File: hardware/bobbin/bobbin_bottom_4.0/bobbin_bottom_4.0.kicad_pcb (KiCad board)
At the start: 2 copper layers, 90.5 x 8.5 mm, 2 parts

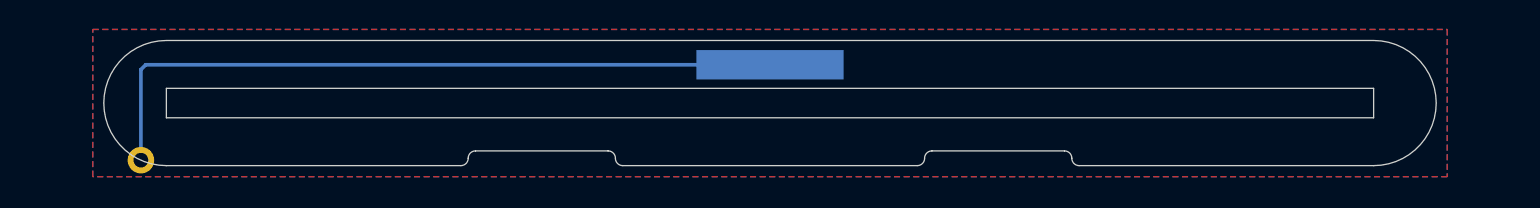
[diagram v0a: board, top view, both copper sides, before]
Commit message: Preamp, Tone Block, Passive, and Bobbin Panel updates
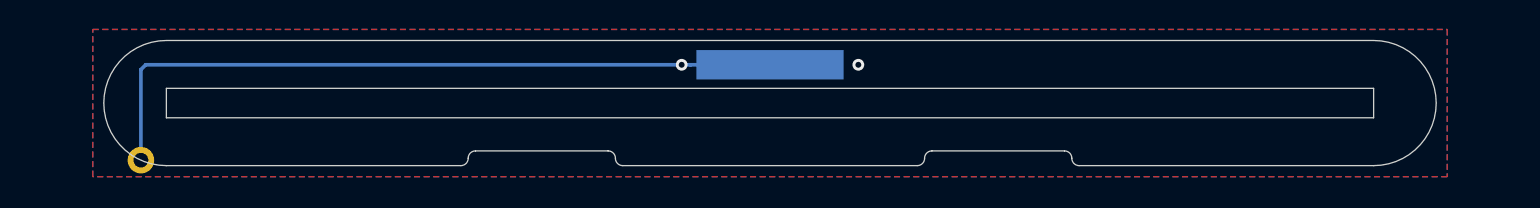
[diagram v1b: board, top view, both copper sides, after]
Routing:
- net GND: vias 0 -> 2
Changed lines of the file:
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@@
     (thickness 1.6)
     (drawings 52)
-    (tracks 3)
+    (tracks 6)
     (zones 0)
     (modules 2)
@@
   (segment (start 87.27 98.73) (end 87.27 104.517267) (width 0.25) (layer B.Cu) (net 1))
   (segment (start 87.6 98.4) (end 87.27 98.73) (width 0.25) (layer B.Cu) (net 1))
-  (segment (start 130 98.4) (end 87.6 98.4) (width 0.25) (layer B.Cu) (net 1))
+  (segment (start 130 98.4) (end 124.6 98.4) (width 0.25) (layer B.Cu) (net 1))
+  (segment (start 124.6 98.4) (end 87.6 98.4) (width 0.25) (layer B.Cu) (net 1))
+  (via (at 124 98.4) (size 0.8) (drill 0.4) (layers F.Cu B.Cu) (net 1))
+  (via (at 136 98.4) (size 0.8) (drill 0.4) (layers F.Cu B.Cu) (net 1))
   (zone (net 1) (net_name GND) (layer F.Cu) (hatch edge 0.508)
     (connect_pads yes (clearance 0.25))

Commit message: 3.5 and 4.0 bottom bobbin updates
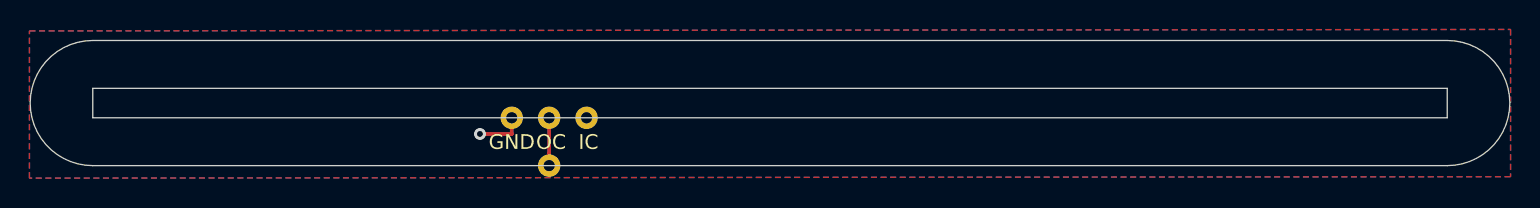
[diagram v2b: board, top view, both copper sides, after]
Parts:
- removed H3: single_pad_smd, cycfi_library:round-single-pad-1.8mm-th
- removed H4: Core GND, cycfi_library:single-pad-10x2
- added J1: Conn_01x01, cycfi_library:xr2-oc-coil-connector, F.Cu at (115.0, 105.2)
- added J2: Conn_01x03, cycfi_library:xr2-coil-connector, F.Cu at (115.0, 102.0)
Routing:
- net GND: track 48.7 -> 2.91 mm, vias 2 -> 1
- net /OC: track 0.00 -> 2.55 mm
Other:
- board size 90.5 x 8.5 mm -> 100.5 x 8.5 mm

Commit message: Copied 3.3" files over
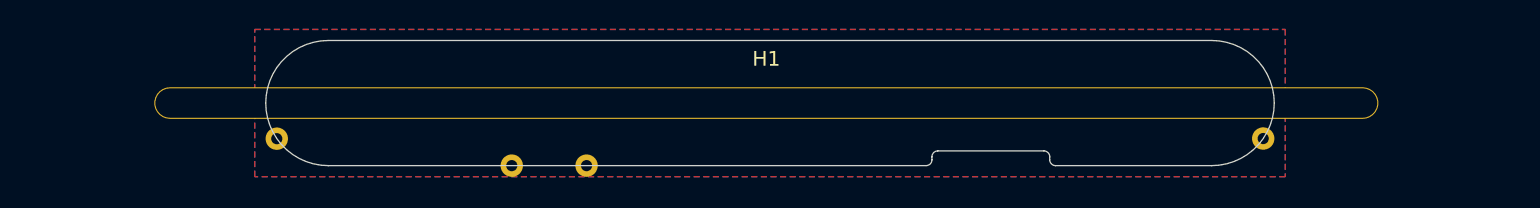
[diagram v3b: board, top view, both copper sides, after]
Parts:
- added H1: single_pad, xr_spectra_library:rail_slot_4.0, F.Cu at (129.8, 101.0)
- added J3: IC, cycfi_library:single-pad-1.52x1.52-th, F.Cu at (96.5, 103.4)
- added J4: IC, cycfi_library:single-pad-1.52x1.52-th, F.Cu at (112.5, 105.2)
- J1: value Conn_01x01 -> OC; footprint cycfi_library:xr2-oc-coil-connector -> cycfi_library:single-pad-1.52x1.52-th
- J2: value Conn_01x03 -> OC; footprint cycfi_library:xr2-coil-connector -> cycfi_library:single-pad-1.52x1.52-th
- moved J2 48.5 mm to (163.5, 103.4), turned to 180 degrees
- moved J1 2.54 mm to (117.5, 105.2)
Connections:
- J2 pad 1: GND -> /OC
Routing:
- net GND: track 2.91 -> 0.00 mm, vias 1 -> 0
- net /OC: track 2.55 -> 0.00 mm
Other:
- board size 100.5 x 8.5 mm -> 68.5 x 8.5 mm
- net class Default removed

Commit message: 3.5" and 4.0" bottom bobbin PCB layout
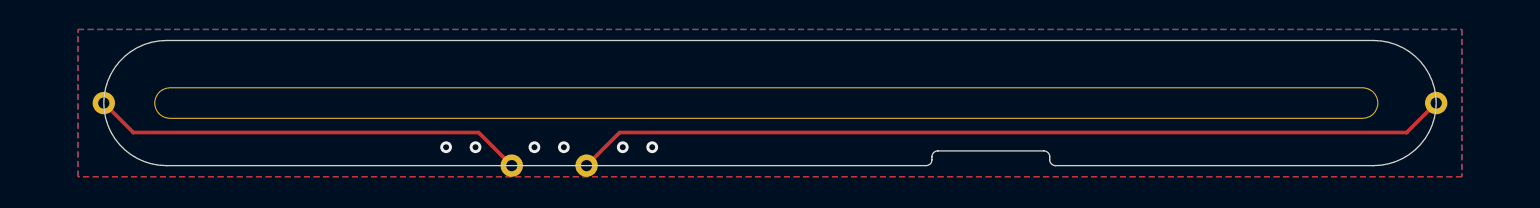
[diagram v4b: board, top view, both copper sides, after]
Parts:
- moved J3 12.0 mm to (84.8, 101.0)
- moved J2 12.0 mm to (175.2, 101.0)
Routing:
- net /OC: track 0.00 -> 59.5 mm
- net /IC: track 0.00 -> 29.5 mm
- net GND: vias 0 -> 6
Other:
- board size 68.5 x 8.5 mm -> 90.5 x 8.5 mm
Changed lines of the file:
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@@
   )
   (footprint "cycfi_library:single-pad-1.52x1.52-th" (layer "F.Cu")
-    (at 163.5 103.41 180)
+    (at 175.25 101 180)
     (property "Sheetfile" "bobbin_bottom_4.0.kicad_sch")
     (property "Sheetname" "")
@@
   )
   (footprint "cycfi_library:single-pad-1.52x1.52-th" (layer "F.Cu")
-    (at 96.5 103.42)
+    (at 84.75 101)
     (property "Sheetfile" "bobbin_bottom_4.0.kicad_sch")
     (property "Sheetname" "")
@@
     (property "Sheetname" "")
     (attr through_hole)
-    (fp_text reference "H1" (at 0 -3 unlocked) (layer "F.SilkS")
+    (fp_text reference "H1" (at 0 -3 unlocked) (layer "F.SilkS") hide
       (effects (font (size 1 1) (thickness 0.15)))
     )
@@
       (net 3 "/IC") (pinfunction "Pin_1") (pintype "passive"))
   )
+  (gr_line (start 171 100) (end 171 102) (layer "Dwgs.User") (width 0.01))
+  (gr_arc (start 141 104.85) (mid 140.882843 105.132843) (end 140.6 105.25) (layer "Dwgs.User") (width 0.01))
+  (gr_line (start 141.4 104.25) (end 148.6 104.25) (layer "Dwgs.User") (width 0.01))
+  (gr_line (start 140.6 105.25) (end 89 105.25) (layer "Dwgs.User") (width 0.01))
+  (gr_line (start 141 104.85) (end 141 104.65) (layer "Dwgs.User") (width 0.01))
+  (gr_arc (start 111.698 105.25) (mid 112.46 104.488) (end 113.222 105.25) (layer "Dwgs.User") (width 0.01))
+  (gr_arc (start 89 105.25) (mid 84.75 101) (end 89 96.75) (layer "Dwgs.User") (width 0.01))
+  (gr_line (start 171 105.25) (end 149.4 105.25) (layer "Dwgs.User") (width 0.01))
+  (gr_arc (start 171 96.75) (mid 175.25 101) (end 171 105.25) (layer "Dwgs.User") (width 0.01))
+  (gr_line (start 89 100) (end 89 102) (layer "Dwgs.User") (width 0.01))
+  (gr_line (start 149 104.65) (end 149 104.85) (layer "Dwgs.User") (width 0.01))
+  (gr_arc (start 116.778 105.25) (mid 117.54 104.488) (end 118.302 105.25) (layer "Dwgs.User") (width 0.01))
   (gr_arc (start 149.4 105.25) (mid 149.117157 105.132843) (end 149 104.85) (layer "Dwgs.User") (width 0.01))
-  (gr_arc (start 160 96.75) (mid 164.25 101) (end 160 105.25) (layer "Dwgs.User") (width 0.01))
-  (gr_line (start 100 100) (end 100 102) (layer "Dwgs.User") (width 0.01))
-  (gr_line (start 100 96.75) (end 160 96.75) (layer "Dwgs.User") (width 0.01))
-  (gr_line (start 100 102) (end 160 102) (layer "Dwgs.User") (width 0.01))
+  (gr_arc (start 175.181689 101.758932) (mid 174.488 101) (end 175.181689 100.241068) (layer "Dwgs.User") (width 0.01))
+  (gr_line (start 89 100) (end 171 100) (layer "Dwgs.User") (width 0.01))
+  (gr_line (start 89 96.75) (end 171 96.75) (layer "Dwgs.User") (width 0.01))
+  (gr_line (start 89 102) (end 171 102) (layer "Dwgs.User") (width 0.01))
   (gr_arc (start 141 104.65) (mid 141.117157 104.367157) (end 141.4 104.25) (layer "Dwgs.User") (width 0.01))
   (gr_arc (start 148.6 104.25) (mid 148.882843 104.367157) (end 149 104.65) (layer "Dwgs.User") (width 0.01))
-  (gr_arc (start 111.698 105.25) (mid 112.46 104.488) (end 113.222 105.25) (layer "Dwgs.User") (width 0.01))
-  (gr_line (start 149 104.65) (end 149 104.85) (layer "Dwgs.User") (width 0.01))
-  (gr_arc (start 116.778 105.25) (mid 117.54 104.488) (end 118.302 105.25) (layer "Dwgs.User") (width 0.01))
-  (gr_line (start 160 105.25) (end 149.4 105.25) (layer "Dwgs.User") (width 0.01))
-  (gr_line (start 141 104.85) (end 141 104.65) (layer "Dwgs.User") (width 0.01))
-  (gr_line (start 160 100) (end 160 102) (layer "Dwgs.User") (width 0.01))
-  (gr_arc (start 96.125734 102.747159) (mid 97.12753 102.978649) (end 96.986778 103.997164) (layer "Dwgs.User") (width 0.01))
-  (gr_line (start 100 100) (end 160 100) (layer "Dwgs.User") (width 0.01))
-  (gr_arc (start 141 104.85) (mid 140.882843 105.132843) (end 140.6 105.25) (layer "Dwgs.User") (width 0.01))
-  (gr_line (start 140.6 105.25) (end 100 105.25) (layer "Dwgs.User") (width 0.01))
-  (gr_arc (start 163.013222 103.997164) (mid 162.872472 102.97865) (end 163.874266 102.747159) (layer "Dwgs.User") (width 0.01))
-  (gr_arc (start 100 105.25) (mid 95.75 101) (end 100 96.75) (layer "Dwgs.User") (width 0.01))
-  (gr_line (start 141.4 104.25) (end 148.6 104.25) (layer "Dwgs.User") (width 0.01))
-  (gr_arc (start 148.6 104.25) (mid 148.882843 104.367157) (end 149 104.65) (layer "Edge.Cuts") (width 0.01))
-  (gr_line (start 141 104.85) (end 141 104.65) (layer "Edge.Cuts") (width 0.01))
+  (gr_arc (start 84.818311 100.241068) (mid 85.512 101) (end 84.818311 101.758932) (layer "Dwgs.User") (width 0.01))
   (gr_line (start 149 104.65) (end 149 104.85) (layer "Edge.Cuts") (width 0.01))
   (gr_arc (start 141 104.85) (mid 140.882843 105.132843) (end 140.6 105.25) (layer "Edge.Cuts") (width 0.01))
+  (gr_line (start 140.6 105.25) (end 89 105.25) (layer "Edge.Cuts") (width 0.01))
+  (gr_arc (start 149.4 105.25) (mid 149.117157 105.132843) (end 149 104.85) (layer "Edge.Cuts") (width 0.01))
+  (gr_line (start 141.4 104.25) (end 148.6 104.25) (layer "Edge.Cuts") (width 0.01))
+  (gr_line (start 89 96.75) (end 171 96.75) (layer "Edge.Cuts") (width 0.01))
+  (gr_line (start 171 105.25) (end 149.4 105.25) (layer "Edge.Cuts") (width 0.01))
   (gr_arc (start 141 104.65) (mid 141.117157 104.367157) (end 141.4 104.25) (layer "Edge.Cuts") (width 0.01))
-  (gr_line (start 100 96.75) (end 160 96.75) (layer "Edge.Cuts") (width 0.01))
-  (gr_arc (start 100 105.25) (mid 95.75 101) (end 100 96.75) (layer "Edge.Cuts") (width 0.01))
-  (gr_line (start 141.4 104.25) (end 148.6 104.25) (layer "Edge.Cuts") (width 0.01))
-  (gr_arc (start 149.4 105.25) (mid 149.117157 105.132843) (end 149 104.85) (layer "Edge.Cuts") (width 0.01))
-  (gr_line (start 140.6 105.25) (end 100 105.25) (layer "Edge.Cuts") (width 0.01))
-  (gr_line (start 160 105.25) (end 149.4 105.25) (layer "Edge.Cuts") (width 0.01))
-  (gr_arc (start 160 96.75) (mid 164.25 101) (end 160 105.25) (layer "Edge.Cuts") (width 0.01))
+  (gr_arc (start 148.6 104.25) (mid 148.882843 104.367157) (end 149 104.65) (layer "Edge.Cuts") (width 0.01))
+  (gr_arc (start 89 105.25) (mid 84.75 101) (end 89 96.75) (layer "Edge.Cuts") (width 0.01))
+  (gr_line (start 141 104.85) (end 141 104.65) (layer "Edge.Cuts") (width 0.01))
+  (gr_arc (start 171 96.75) (mid 175.25 101) (end 171 105.25) (layer "Edge.Cuts") (width 0.01))
+  (via (at 120 104) (size 0.8) (drill 0.4) (layers "F.Cu" "B.Cu") (free) (net 1))
+  (via (at 122 104) (size 0.8) (drill 0.4) (layers "F.Cu" "B.Cu") (free) (net 1))
+  (via (at 116 104) (size 0.8) (drill 0.4) (layers "F.Cu" "B.Cu") (free) (net 1))
+  (via (at 108 104) (size 0.8) (drill 0.4) (layers "F.Cu" "B.Cu") (free) (net 1))
+  (via (at 110 104) (size 0.8) (drill 0.4) (layers "F.Cu" "B.Cu") (free) (net 1))
+  (via (at 114 104) (size 0.8) (drill 0.4) (layers "F.Cu" "B.Cu") (free) (net 1))
+  (segment (start 173.25 103) (end 119.79 103) (width 0.25) (layer "F.Cu") (net 2))
+  (segment (start 119.79 103) (end 117.54 105.25) (width 0.25) (layer "F.Cu") (net 2))
+  (segment (start 175.25 101) (end 173.25 103) (width 0.25) (layer "F.Cu") (net 2))
+  (segment (start 84.75 101) (end 86.75 103) (width 0.25) (layer "F.Cu") (net 3))
+  (segment (start 86.75 103) (end 110.21 103) (width 0.25) (layer "F.Cu") (net 3))
+  (segment (start 110.21 103) (end 112.46 105.25) (width 0.25) (layer "F.Cu") (net 3))
   (zone (net 1) (net_name "GND") (layer "F.Cu") (hatch edge 0.508)
     (connect_pads (clearance 0.25))
     (min_thickness 0.254) (filled_areas_thickness no)
-    (fill (thermal_gap 0.508) (thermal_bridge_width 0.508))
+    (fill yes (thermal_gap 0.508) (thermal_bridge_width 0.508))
     (polygon
       (pts
-        (xy 165 106)
-        (xy 95 106)
-        (xy 95 96)
-        (xy 165 96)
+        (xy 177 106)
+        (xy 83 106)
+        (xy 83 96)
+        (xy 177 96)
       )
     )
@@
     (connect_pads (clearance 0.25))
     (min_thickness 0.254) (filled_areas_thickness no)
-    (fill (thermal_gap 0.508) (thermal_bridge_width 0.508))
+    (fill yes (thermal_gap 0.508) (thermal_bridge_width 0.508))
     (polygon
       (pts
-        (xy 165 106)
-        (xy 95 106)
-        (xy 95 96)
-        (xy 165 96)
+        (xy 177 106)
+        (xy 83 106)
+        (xy 83 96)
+        (xy 177 96)
       )
     )
